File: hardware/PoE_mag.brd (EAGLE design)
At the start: 149.9 x 124.5 mm, 124 parts, among them IC1 LD1117V33, IC10 74LVC1T45SOT23-HAND, IC11 PCA9517A, IC2 LD1117V33, IC3 DS1338, IC4 ATMEGA1284, IC5 TSR 1-2450, IC6 MCP2200, IC7 74LVC1T45SOT23-HAND, IC8 74LVC1T45SOT23-HAND, IC9 74LVC1T45SOT23-HAND, Q1 BSS138, Q2 BUK98150-55A, X1 PWR, X2 JTAG, X3 USB, X4 MICRO-SD-SOCKETHIROSE-DM3D, X5 CONN-SMATHD, X6 UFL, X7 22-23-2021, X8 RJ45, X9 RJ11, Y1 32k768, Y2 16MHz, Y3 12MHz

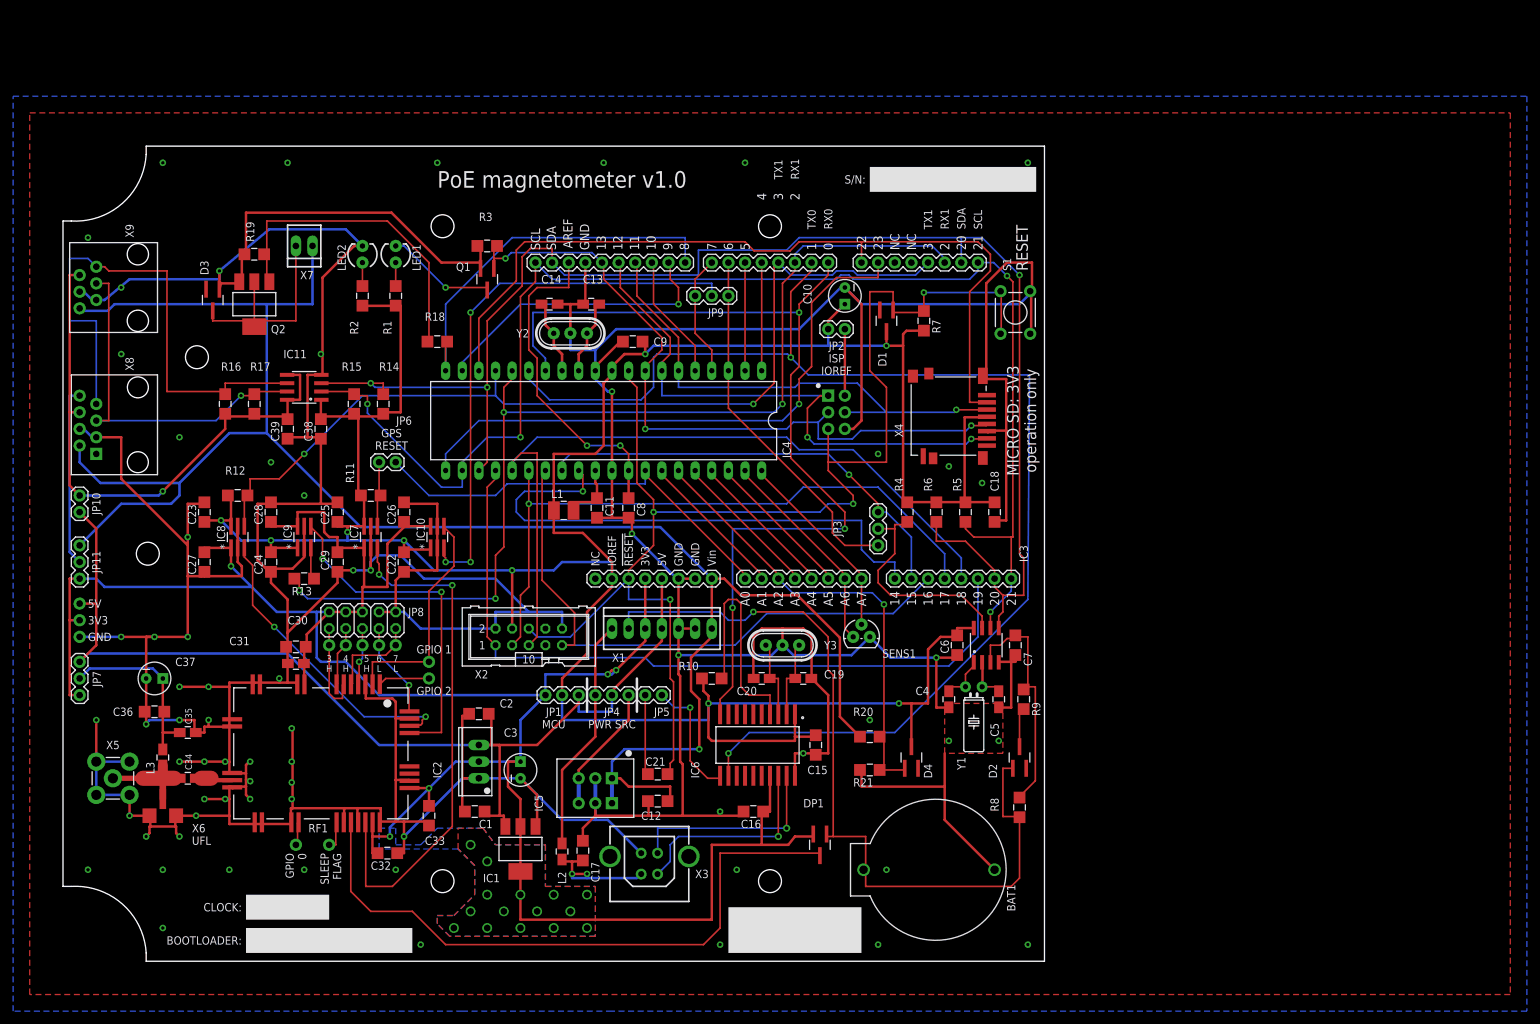
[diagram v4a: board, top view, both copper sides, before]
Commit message: Minor changes for ground pour
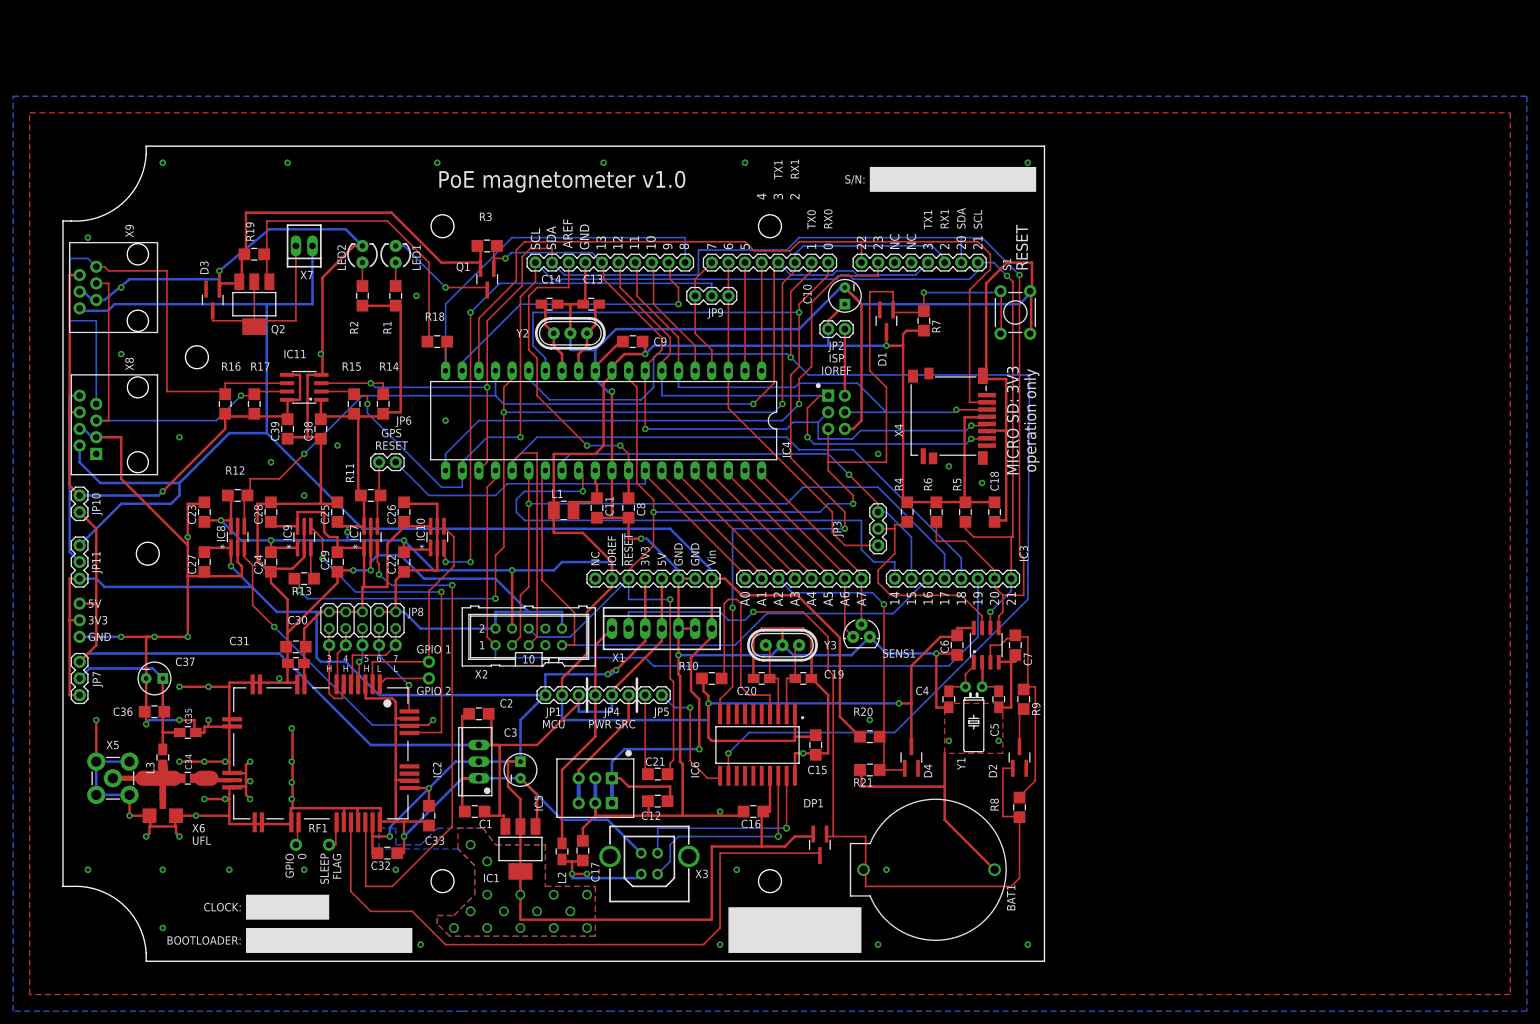
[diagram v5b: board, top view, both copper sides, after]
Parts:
- R14, R15, R16, R17: value 10k -> 4k7
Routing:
- net GPS_RX1: track 46.1 -> 48.7 mm
- net GND: track 1185.0 -> 1187.2 mm, vias 68 -> 71
- net VCC: track 465.0 -> 463.5 mm
- net VIN: track 293.9 -> 294.6 mm

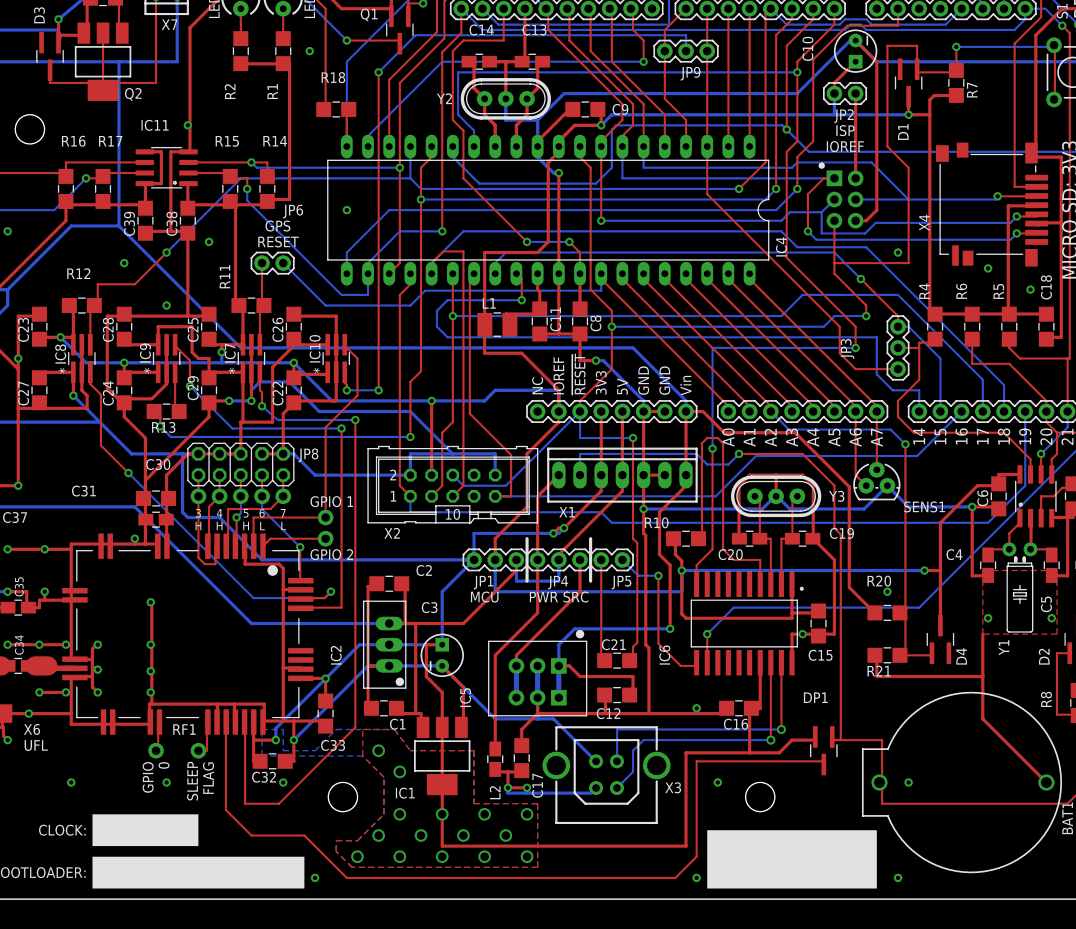
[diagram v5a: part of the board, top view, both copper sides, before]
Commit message: Always power LM61 and swap to SOT23 package
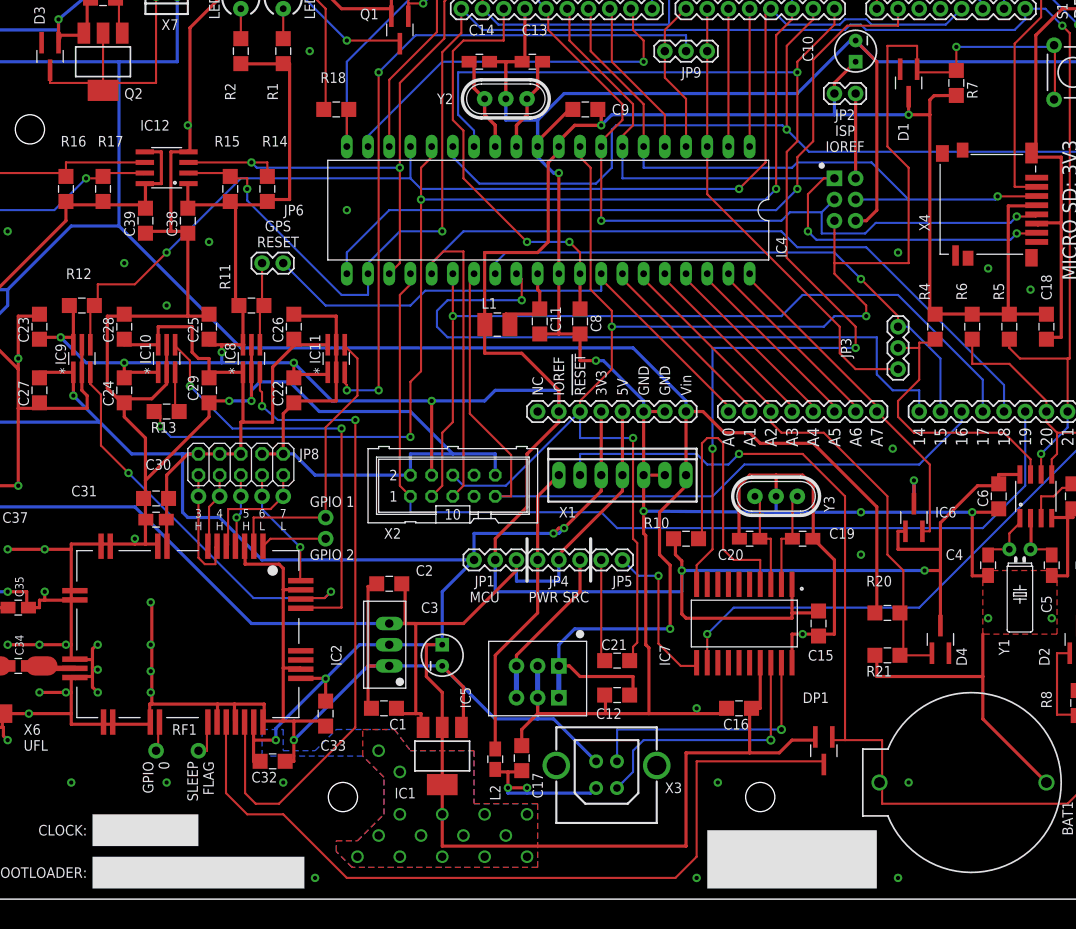
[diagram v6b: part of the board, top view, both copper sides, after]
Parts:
- removed SENS1: LM61, SteveMarple:TO-92
- added IC12: PCA9517A, SteveMarple:SO08
- IC11: value PCA9517A -> 74LVC1T45SOT23-HAND; device SteveMarple:SO08 -> SteveMarple:SOT23-6-HAND
- IC6: value MCP2200 -> LM61; device SteveMarple:SO20 -> SteveMarple:SOT23-3-HAND
- IC7: value 74LVC1T45SOT23-HAND -> MCP2200; device SteveMarple:SOT23-6-HAND -> SteveMarple:SO20
- moved IC7 67.0 mm to (106.0, 20.3), turned to 180 degrees
- moved IC11 30.6 mm to (57.1, 52.1)
- moved IC6 24.0 mm to (126.4, 33.0), turned to 90 degrees
- moved IC10 20.3 mm to (36.8, 52.1)
- moved IC8 20.3 mm to (47.0, 52.1)
- moved IC9 10.2 mm to (26.7, 52.1)
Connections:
- net !GPS_RESET: now also IC8.3; no longer IC7.3
- net !MCP2200_RESET: now also IC7.4; no longer IC6.4
- net +3V3: now also IC11.6, IC7.17, IC9.1; no longer IC6.17, IC7.1, IC9.6
- net 0(RX0): now also IC7.10; no longer IC6.10
- net 1(TX0): now also IC7.12; no longer IC6.12
- net 20(SDA): now also IC12.3; no longer IC11.3
- net 21(SCL): now also IC12.2; no longer IC11.2
- net 3(TX1): now also IC9.4; no longer IC8.4
- net A6: no longer SENS1.1
- net A7: now also IC6.2; no longer SENS1.2
- net AUTO_RESET: now also IC7.11; no longer IC6.11
- net GND: now also IC11.2, IC11.5, IC12.4, IC6.3, IC7.20; no longer IC11.4, IC6.20, IC7.2, IC7.5, SENS1.3
- net GPIO1: now also IC11.4; no longer IC10.4
- net GPS_RX1: now also IC9.3; no longer IC8.3
- net GPS_TX1: now also IC10.4; no longer IC9.4
- net MAG_SCL: now also IC12.7; no longer IC11.7
- net MAG_SDA: now also IC12.6; no longer IC11.6
- net MAG_VCC: now also IC12.5, IC12.8; no longer IC11.5, IC11.8
- net N$18: now also IC7.2; no longer IC6.2
- net N$22: now also IC8.4; no longer IC7.4
- net N$25: now also IC10.3; no longer IC9.3
- net N$7: now also IC7.3; no longer IC6.3
- net PPS: now also IC11.3; no longer IC10.3
- net USB_D+: now also IC7.19; no longer IC6.19
- net USB_D-: now also IC7.18; no longer IC6.18
- net VCC: now also IC12.1, IC7.1, IC9.6; no longer IC7.6, IC9.1
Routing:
- net A7: track 29.8 -> 40.7 mm
- net A6: track 32.2 -> 22.8 mm
- net VCC: track 463.5 -> 471.6 mm
- net GND: track 1187.2 -> 1192.2 mm, vias 71 -> 74
- net A2: track 70.6 -> 66.1 mm, vias 1 -> 0
- net V_BACKUP: track 98.5 -> 97.3 mm
- net VIN: track 294.6 -> 295.5 mm
- net !GPS_RESET: track 79.6 -> 78.8 mm
- net 16(TDI): track 90.9 -> 91.7 mm
- net 19(TCK): track 114.5 -> 115.1 mm

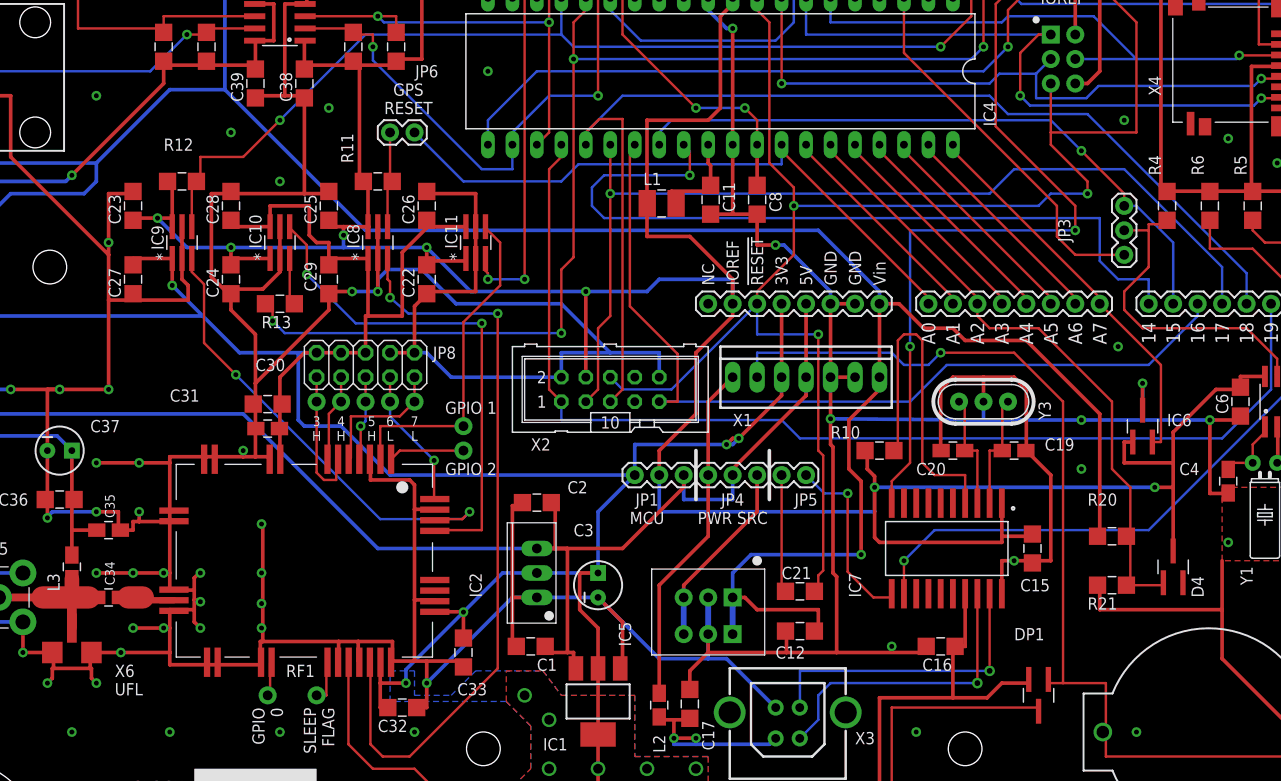
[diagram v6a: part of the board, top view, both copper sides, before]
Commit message: Improve decoupling for voltage regulators
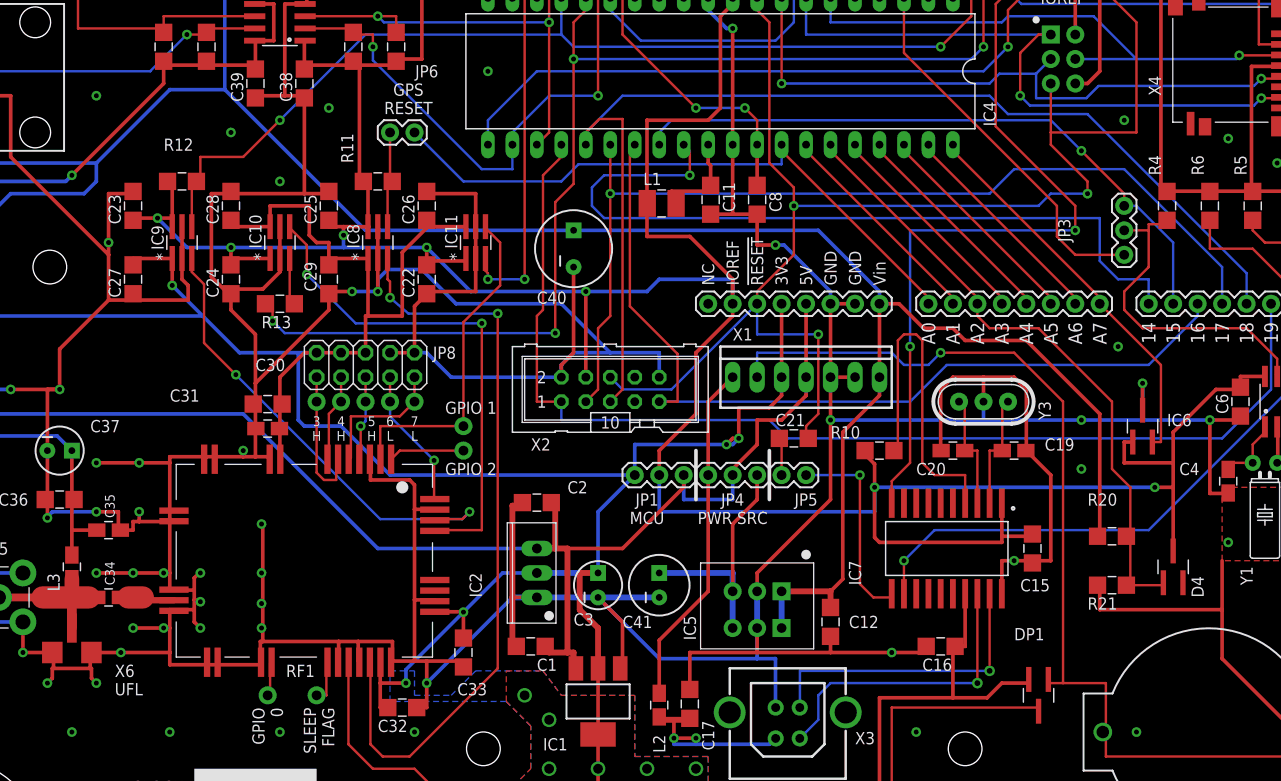
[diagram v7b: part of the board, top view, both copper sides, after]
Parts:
- added C40: 100u 25V, SteveMarple:CPOL-RADIAL-100UF-25V-150MIL
- added C41: 100u, SteveMarple:CPOL-RADIAL-100UF-16V
- C10: value 4u7 -> 10u; device SparkFun:CPOL-RADIAL-10UF-25V -> SteveMarple:CPOL-RADIAL-10UF-25V
- C37: value 4u7 -> 10u
- moved C21 15.9 mm to (90.2, 31.8)
- moved IC5 5.12 mm to (86.4, 15.9)
- moved C12 3.31 mm to (94.0, 12.7), turned to 270 degrees
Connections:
- net GND: now also C40.2, C41.2
- net N$14: now also C41.1
- net VIN: now also C40.1
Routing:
- net VIN: track 295.5 -> 278.1 mm, vias 1 -> 0
- net GND: track 1192.2 -> 1208.1 mm, vias 74 -> 73
- net !RESET: track 204.3 -> 189.3 mm
- net N$15: track 12.2 -> 3.85 mm
- net N$14: track 15.9 -> 22.6 mm
- net 19(TCK): track 115.1 -> 117.6 mm
- net AUTO_RESET: track 19.3 -> 21.2 mm
- net +3V3: track 369.1 -> 370.9 mm
- net +5V: track 169.4 -> 167.7 mm

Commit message: Renumber components
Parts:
- C12: value 1u -> 100u 25V; device SteveMarple:1206-HAND -> SteveMarple:CPOL-RADIAL-100UF-25V-150MIL
- C13, C34, C35: value 22p -> 1u; device SteveMarple:0805-HAND -> SteveMarple:1206-HAND
- C14: value 22p -> 100u; device SteveMarple:0805-HAND -> SteveMarple:CPOL-RADIAL-100UF-16V
- C15, C16, C21, C22: value 100n -> 22p; device SteveMarple:1206-HAND -> SteveMarple:0805-HAND
- C17: value 10n -> 100n
- C19: value 22p -> 10n; device SteveMarple:0805-HAND -> SteveMarple:1206-HAND
- C20, C31: value 22p -> 100n; device SteveMarple:0805-HAND -> SteveMarple:1206-HAND
- C30: value 1u -> 100n
- C33, C36: value 1u -> 22p; device SteveMarple:1206-HAND -> SteveMarple:0805-HAND
- C37: value 10u -> 22p; device SteveMarple:CPOL-RADIAL-10UF-25V -> SteveMarple:0805-HAND
- C38: value 100n -> 1u
- C39: value 100n -> 10u; device SteveMarple:1206-HAND -> SteveMarple:CPOL-RADIAL-10UF-25V
- C40: value 100u 25V -> 100n; device SteveMarple:CPOL-RADIAL-100UF-25V-150MIL -> SteveMarple:1206-HAND
- C41: value 100u -> 100n; device SteveMarple:CPOL-RADIAL-100UF-16V -> SteveMarple:1206-HAND
- moved C16 83.5 mm to (74.3, 87.6), turned to 0 degrees
- moved C13 76.1 mm to (94.0, 12.7), turned to 270 degrees
- moved C15 75.5 mm to (80.6, 87.6), turned to 180 degrees
- moved C23 72.7 mm to (90.2, 31.8), turned to 0 degrees
- moved C14 71.1 mm to (76.2, 16.5), turned to 90 degrees
- moved C41 66.8 mm to (34.3, 68.6), turned to 270 degrees
- moved C18 58.7 mm to (105.4, 10.2), turned to 180 degrees
- moved C22 57.4 mm to (106.7, 30.5), turned to 180 degrees
- moved C38 50.1 mm to (14.0, 25.4), turned to 180 degrees
- moved C12 47.0 mm to (67.3, 51.4), turned to 90 degrees
- moved C20 43.7 mm to (142.2, 55.9), turned to 270 degrees
- moved C39 43.2 mm to (14.0, 30.5), turned to 0 degrees
- moved C19 42.7 mm to (79.4, 4.19), turned to 90 degrees
- moved C17 39.0 mm to (114.9, 20.3), turned to 270 degrees
- moved C35 39.0 mm to (55.9, 9.53), turned to 270 degrees
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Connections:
- net !RESET: now also C23.2; no longer C21.2
- net +3V3: now also C18.1, C34.1, C35.1; no longer C16.1, C26.1, C27.1
- net GND: now also C21.2, C34.2; no longer C23.2, C36.2
- net MAG_VCC: now also C41.1; no longer C39.1
- net N$1: now also C16.1; no longer C14.1
- net N$14: now also C14.1; no longer C41.1
- net N$15: now also C23.1; no longer C21.1
- net N$18: now also C21.1; no longer C19.1
- net N$2: now also C15.1; no longer C13.1
- net N$23: now also C36.2; no longer C34.2
- net N$24: now also C36.1; no longer C34.1
- net N$7: now also C22.1; no longer C20.1
- net VBUS: now also C19.1; no longer C17.1
- net VCC: now also C17.1, C20.1, C26.1, C27.1, C40.1; no longer C15.1, C18.1, C22.1, C23.1, C38.1
- net VIN: now also C13.1; no longer C40.1
- net V_ANT: now also C38.1, C39.1; no longer C35.1, C36.1
